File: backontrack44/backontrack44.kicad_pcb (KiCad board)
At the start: 2 copper layers, 151.8 x 95.6 mm, 98 parts, among them J1 AudioJack4, J2 OLED, SW1-1 choc_SW_HS, SW1-2 choc_SW_HS, SW1-3 choc_SW_HS, SW1-4 choc_SW_HS, SW1-5 choc_SW_HS, SW1-6 choc_SW_HS, SW2-1 choc_SW_HS, SW2-2 choc_SW_HS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

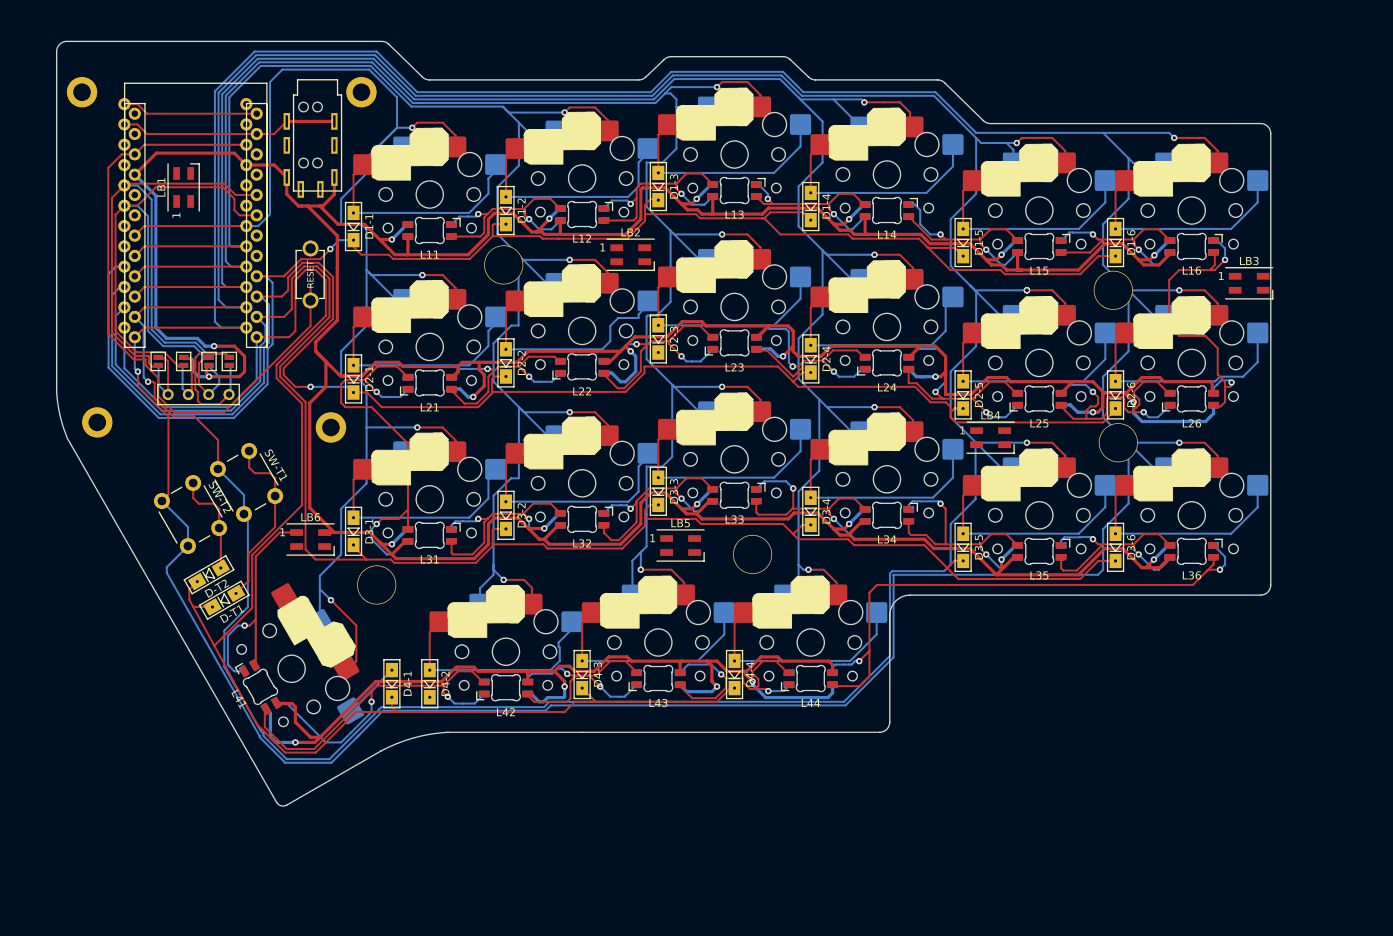
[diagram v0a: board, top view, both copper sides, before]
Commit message: better fitting of the board on the right side
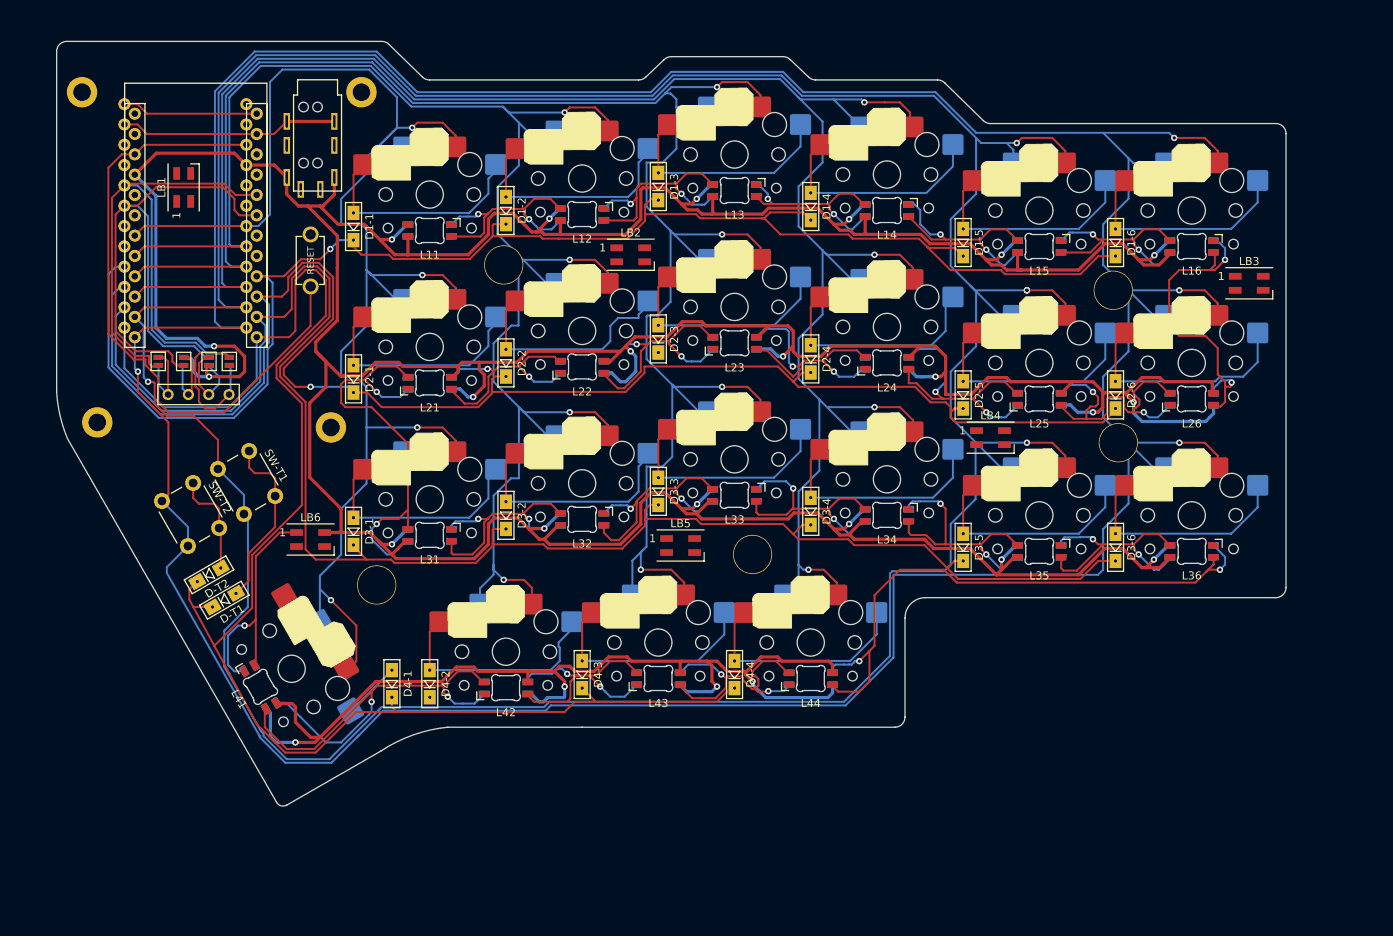
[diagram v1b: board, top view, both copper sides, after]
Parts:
- moved RS1 1.76 mm to (80.0, 50.2)
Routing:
- net Net-(L36-Pad3): track 72.7 -> 74.5 mm
- net VCC: track 774.6 -> 775.7 mm
- net SCL: track 72.7 -> 73.4 mm
- net Net-(J2-Pad4): track 18.6 -> 19.2 mm
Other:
- board size 151.8 x 95.6 mm -> 153.7 x 95.6 mm

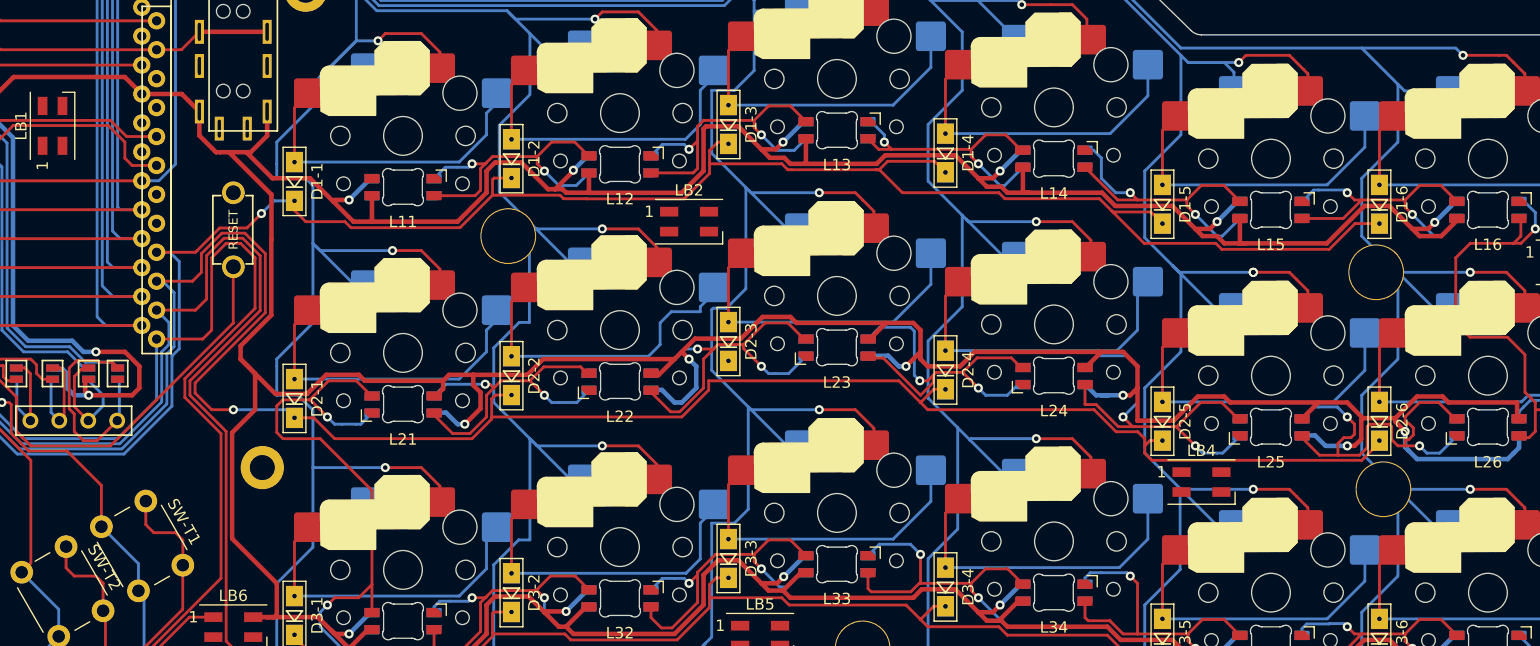
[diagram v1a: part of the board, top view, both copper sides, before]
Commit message: fix overlapping errors
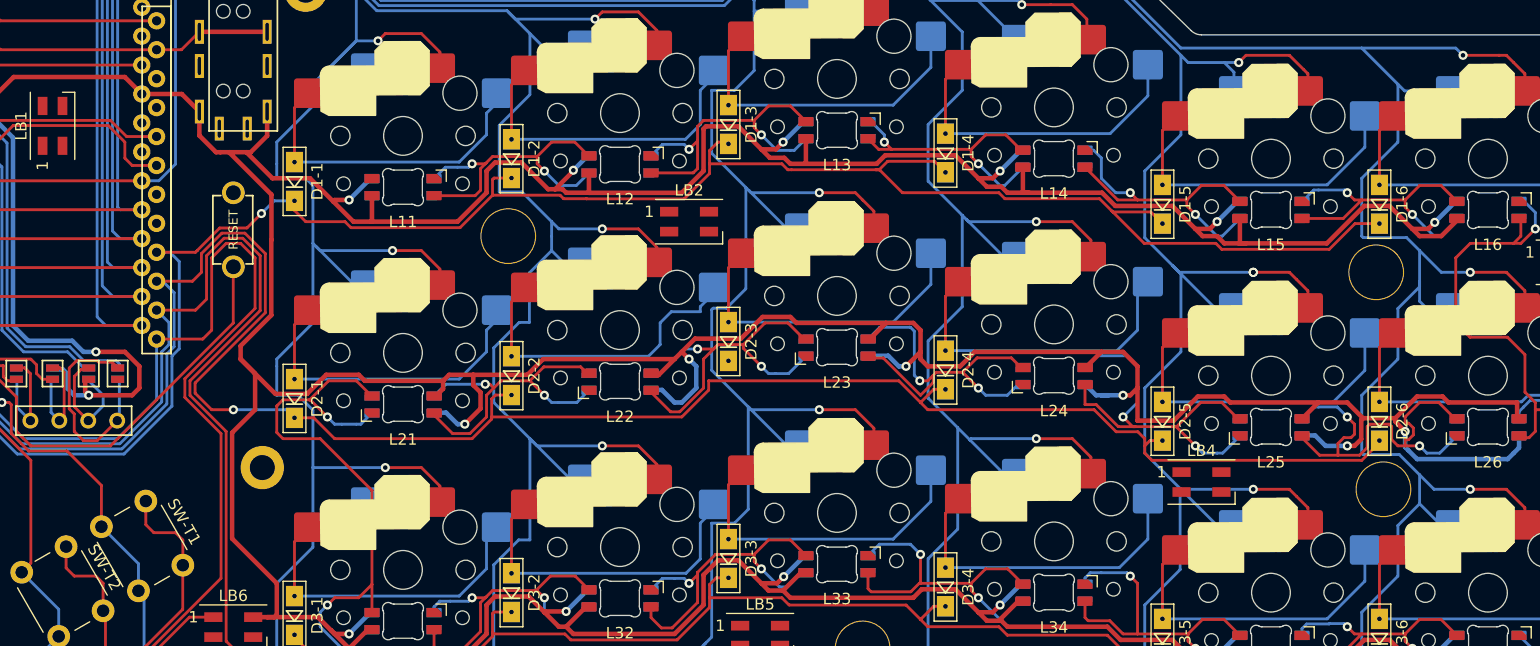
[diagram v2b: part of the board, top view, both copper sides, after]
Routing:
- net col2: track 211.6 -> 210.3 mm
- net col6: track 470.5 -> 471.6 mm

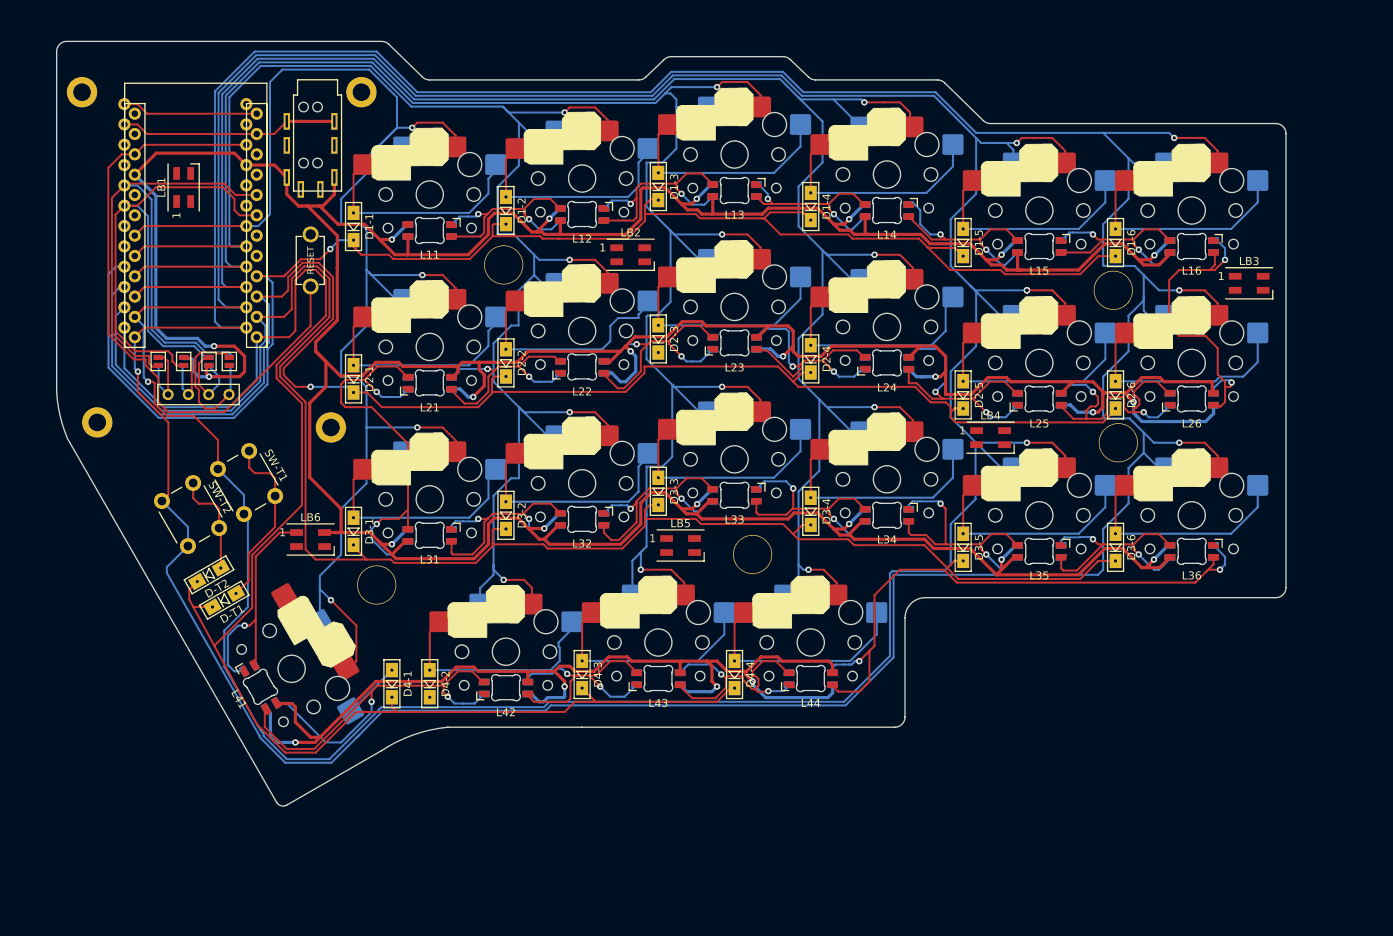
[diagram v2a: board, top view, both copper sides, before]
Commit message: fixed many DRC errors
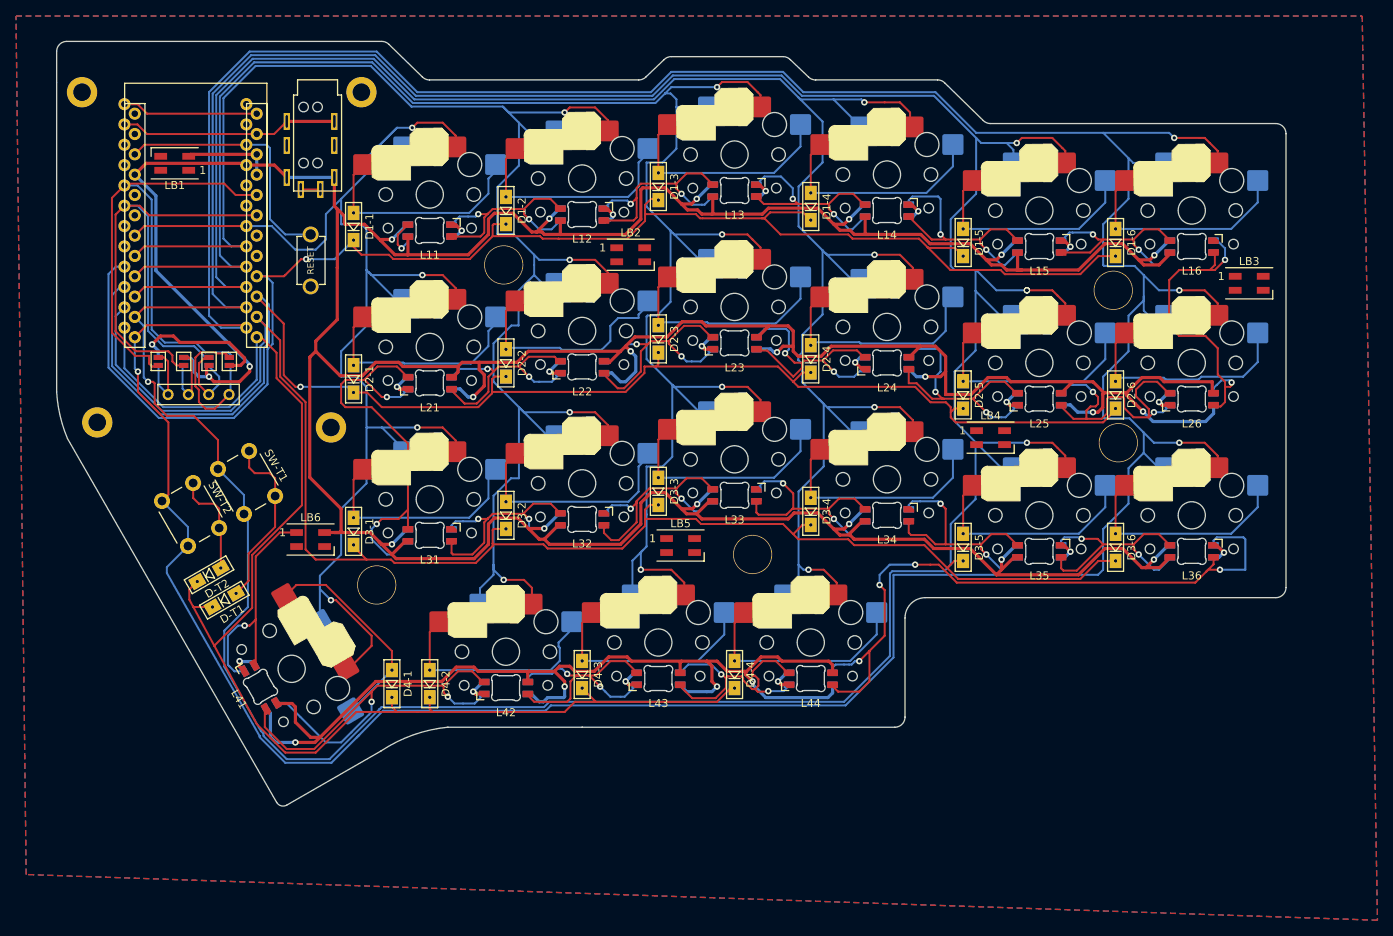
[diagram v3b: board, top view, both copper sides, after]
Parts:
- moved LB1 3.22 mm to (63.0, 38.1), turned to 180 degrees
- turned RS1 to -90 degrees
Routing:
- net GND: track 0.00 -> 83.8 mm, vias 0 -> 18
- net RESET: track 80.4 -> 32.3 mm
- net row4: track 192.7 -> 170.0 mm
- net row3: track 214.1 -> 193.4 mm
- net Net-(D4-1-Pad2): track 7.28 -> 27.1 mm
- net col1: track 194.3 -> 176.1 mm
- net row2: track 194.4 -> 179.7 mm
- net VCC: track 775.7 -> 763.7 mm
- net Net-(L36-Pad3): track 74.5 -> 84.6 mm, vias 2 -> 4
- net Net-(L13-Pad3): track 25.4 -> 33.0 mm
- net unconnected-(L11-Pad2): track 0.00 -> 5.52 mm, vias 0 -> 1
- net SCL: track 73.4 -> 70.7 mm
- net Net-(L14-Pad3): track 30.4 -> 33.1 mm
- net unconnected-(J1-PadS): track 0.00 -> 2.45 mm
- net col5: track 429.7 -> 432.0 mm
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- added copper zone on B.Cu, net GND
- added copper zone on F.Cu, net GND

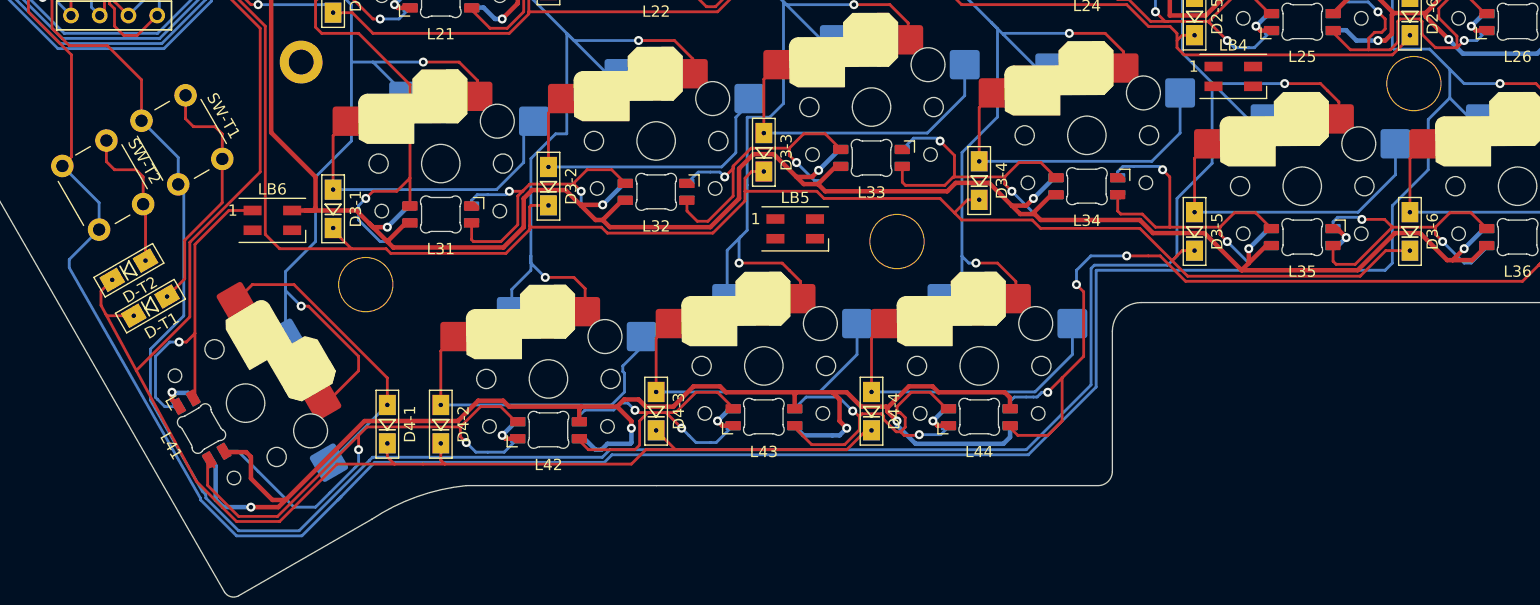
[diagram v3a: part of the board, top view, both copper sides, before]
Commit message: removed col5 and col6 loops
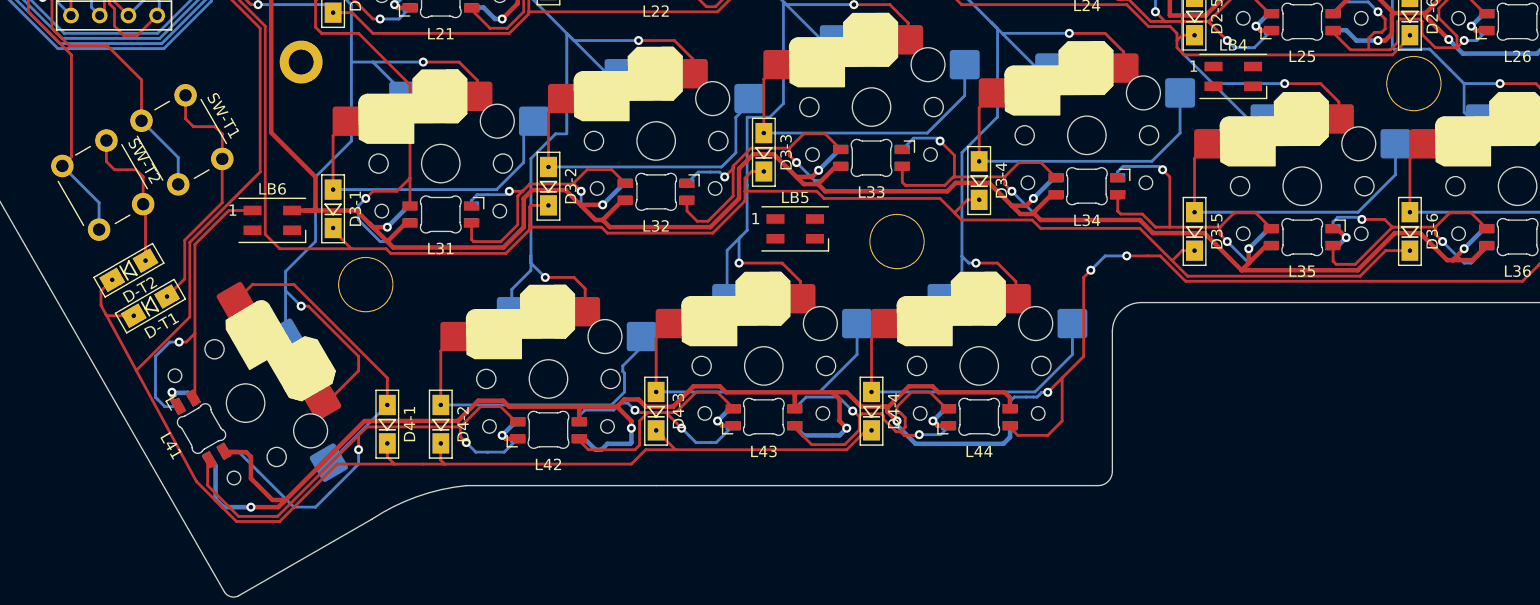
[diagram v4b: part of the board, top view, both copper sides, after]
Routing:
- net col6: track 472.8 -> 303.0 mm
- net col5: track 432.0 -> 282.4 mm
- net Net-(L36-Pad3): track 84.6 -> 83.3 mm
